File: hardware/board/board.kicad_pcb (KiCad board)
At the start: 2 copper layers, 100 x 30 mm, 40 parts, among them J1 DC THRU, J2 DC THRU, J3 DC OUT, J4 DC IN, J5 DC IN, J6 DC OUT, J7 Eurorack Power, J8 Eurorack Power, SW1 ON/OFF, U1 VX7805-500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

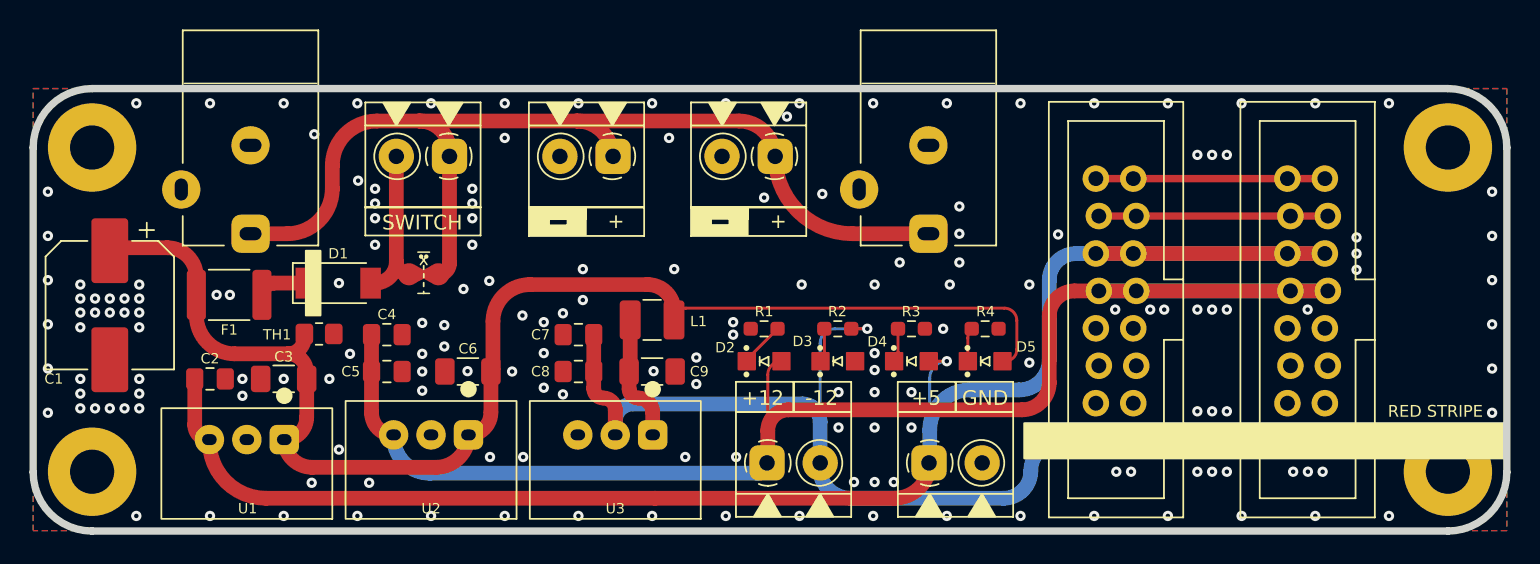
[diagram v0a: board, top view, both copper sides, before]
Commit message: Use new winterbloom footprints
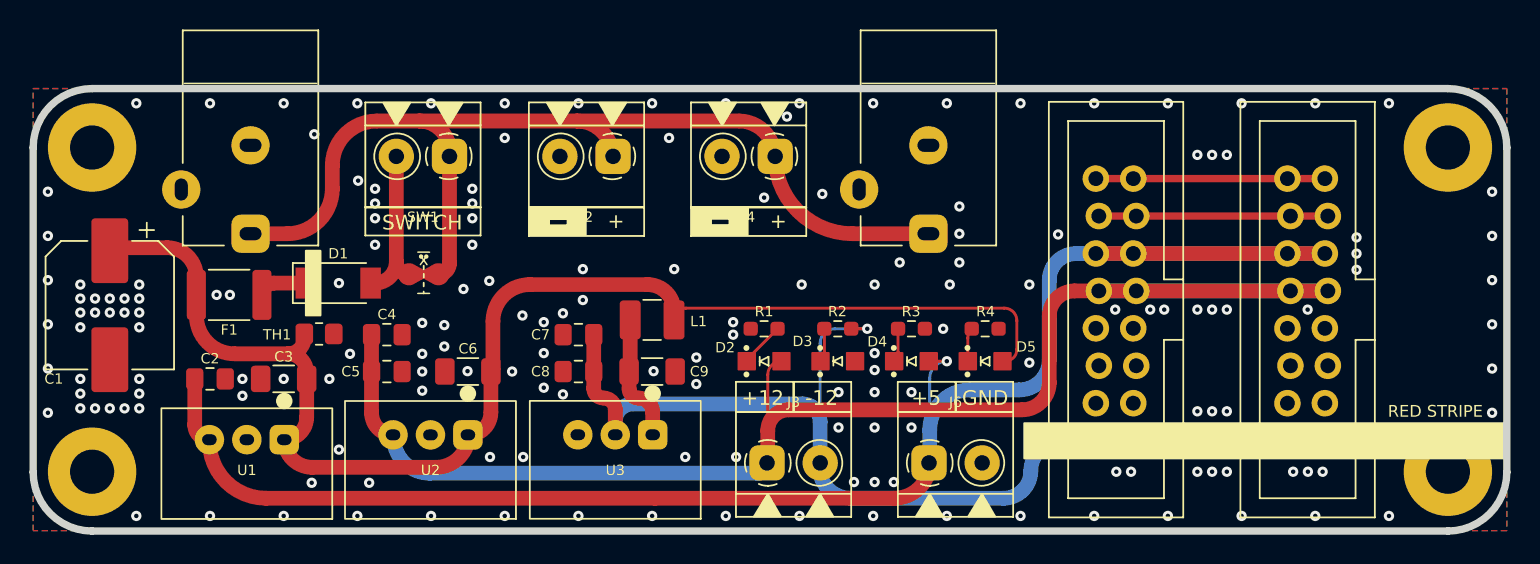
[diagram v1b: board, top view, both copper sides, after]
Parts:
- J2, J3, J4, J6, SW1: footprint winterbloom:TerminalBlock_4Ucon_1x02_P3.50mm_Horizontal -> winterbloom:TerminalBlock_4UCON_1x02_P3.50mm_Horizontal
- J7, J8: footprint winterbloom:IDC-Header_2x08_P2.54mm_Vertical_Press_Fit -> winterbloom:Eurorack_Power_2x8_Shrouded_Lock
- U1: footprint winterbloom:CUI_VX78 -> winterbloom:Converter_DCDC_CUI_VX78-500_THT
- U2, U3: footprint winterbloom:CUI_P78E -> winterbloom:Converter_DCDC_CUI_P78E-1000_THT
- moved U3 3.06 mm to (100.5, 116.6)
- moved U2 3.02 mm to (88.0, 116.6)
- moved U1 3.01 mm to (75.5, 116.9)

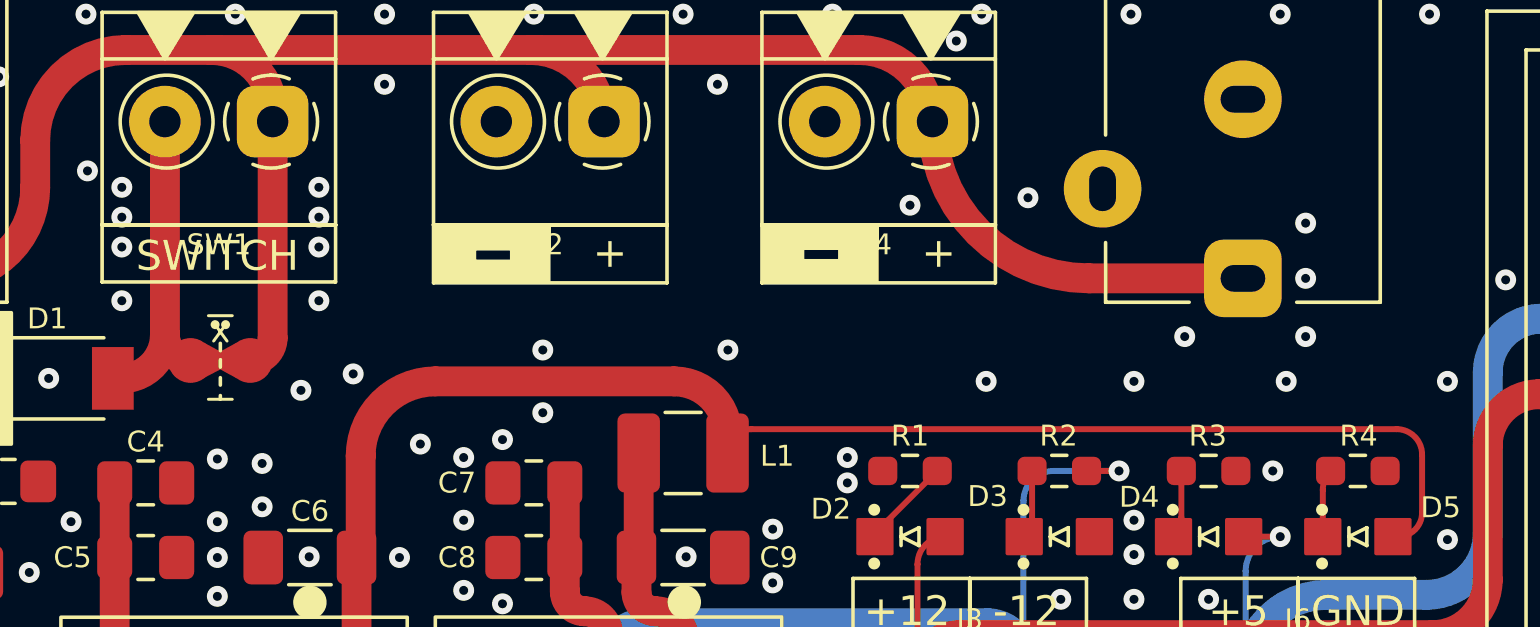
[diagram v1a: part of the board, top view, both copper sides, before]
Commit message: Add OSHW and polarity symbols to the PCB
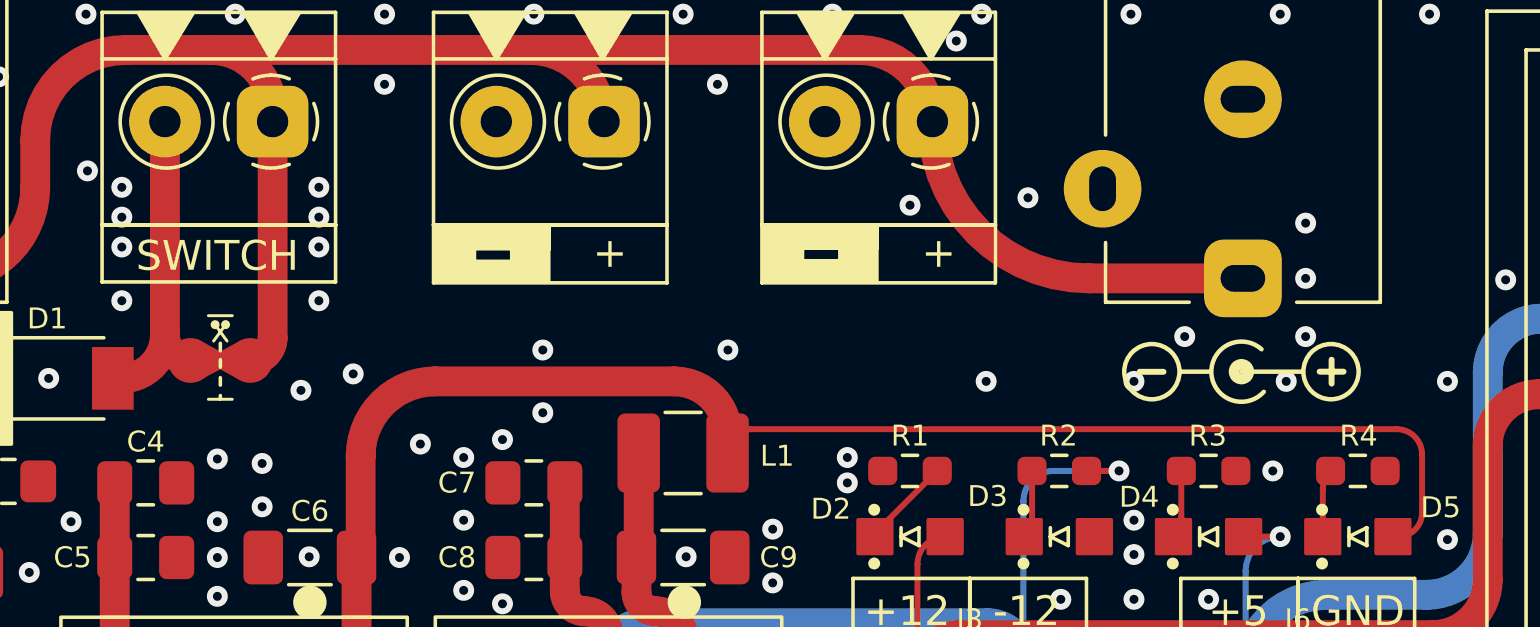
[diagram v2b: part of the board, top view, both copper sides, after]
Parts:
- added REF**: Symbol_Barrel_Polarity, Symbol:Symbol_Barrel_Polarity, F.Cu at (119.2, 106.0)
- added REF**: OSHW-Logo_5.7x6mm_Copper, Symbol:OSHW-Logo_5.7x6mm_Copper, B.Cu at (153.9, 108.5)
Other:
- board text removed: "TRANS RIGHTS"

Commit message: Resolve ERC errors related to non-schematic footprints
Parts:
- renumbered G*** to NICKEL, REF** to OSHW, REF** to POLARITY, G*** to WNTR
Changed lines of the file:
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@@
     (tags "barrel polarity")
     (attr board_only exclude_from_pos_files exclude_from_bom)
-    (fp_text reference "REF**" (at 0 -2) (layer "F.SilkS") hide
+    (fp_text reference "POLARITY" (at 0 -2) (layer "F.SilkS") hide
       (effects (font (size 1 1) (thickness 0.15)))
     )
@@
     (at 105.4 108.075 180)
     (attr board_only exclude_from_pos_files exclude_from_bom)
-    (fp_text reference "G***" (at 0 0) (layer "B.SilkS") hide
+    (fp_text reference "WNTR" (at 0 0) (layer "B.SilkS") hide
       (effects (font (size 1.524 1.524) (thickness 0.3)) (justify mirror))
     )
@@
     (at 65.1 108.075 180)
     (attr board_only exclude_from_pos_files exclude_from_bom)
-    (fp_text reference "G***" (at 0 0) (layer "B.SilkS") hide
+    (fp_text reference "NICKEL" (at 0 0) (layer "B.SilkS") hide
       (effects (font (size 1.524 1.524) (thickness 0.3)) (justify mirror))
     )
@@
     (descr "Open Source Hardware Logo")
     (tags "Logo OSHW")
-    (attr exclude_from_pos_files exclude_from_bom)
-    (fp_text reference "REF**" (at 0 0) (layer "B.SilkS") hide
+    (attr board_only exclude_from_pos_files exclude_from_bom)
+    (fp_text reference "OSHW" (at 0 0) (layer "B.SilkS") hide
       (effects (font (size 1 1) (thickness 0.15)) (justify mirror))
     )

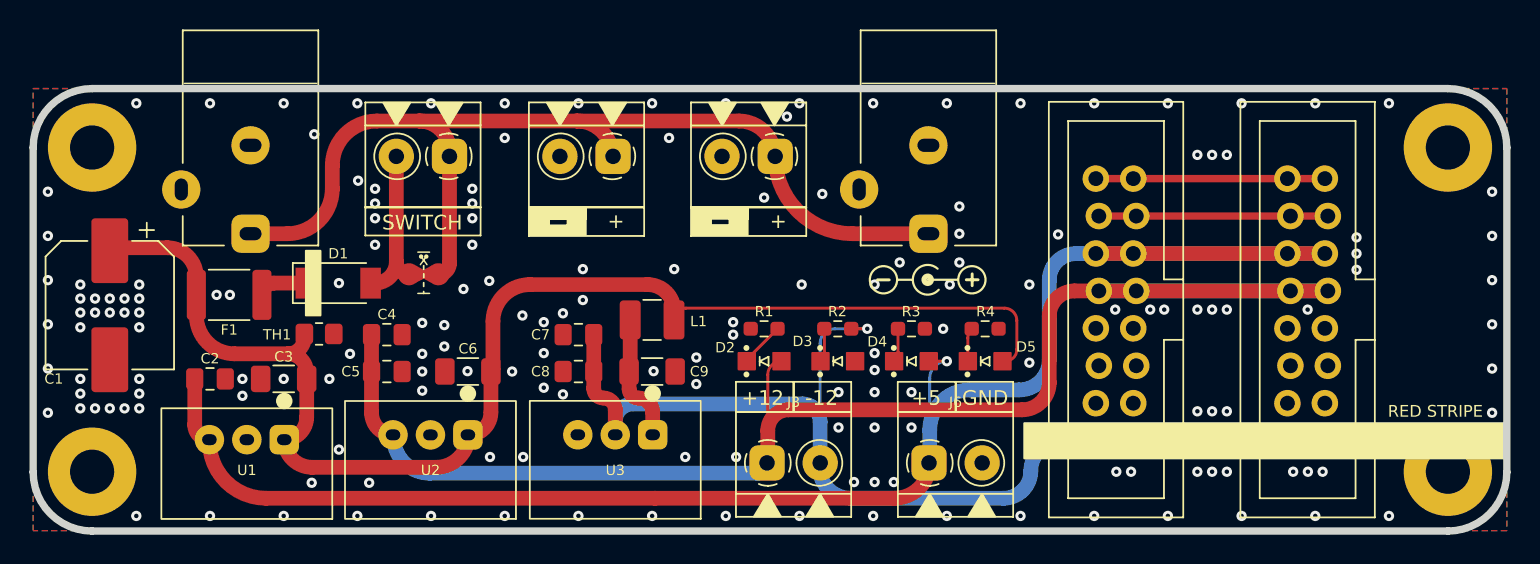
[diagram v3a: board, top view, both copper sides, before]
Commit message: Use hatched fills
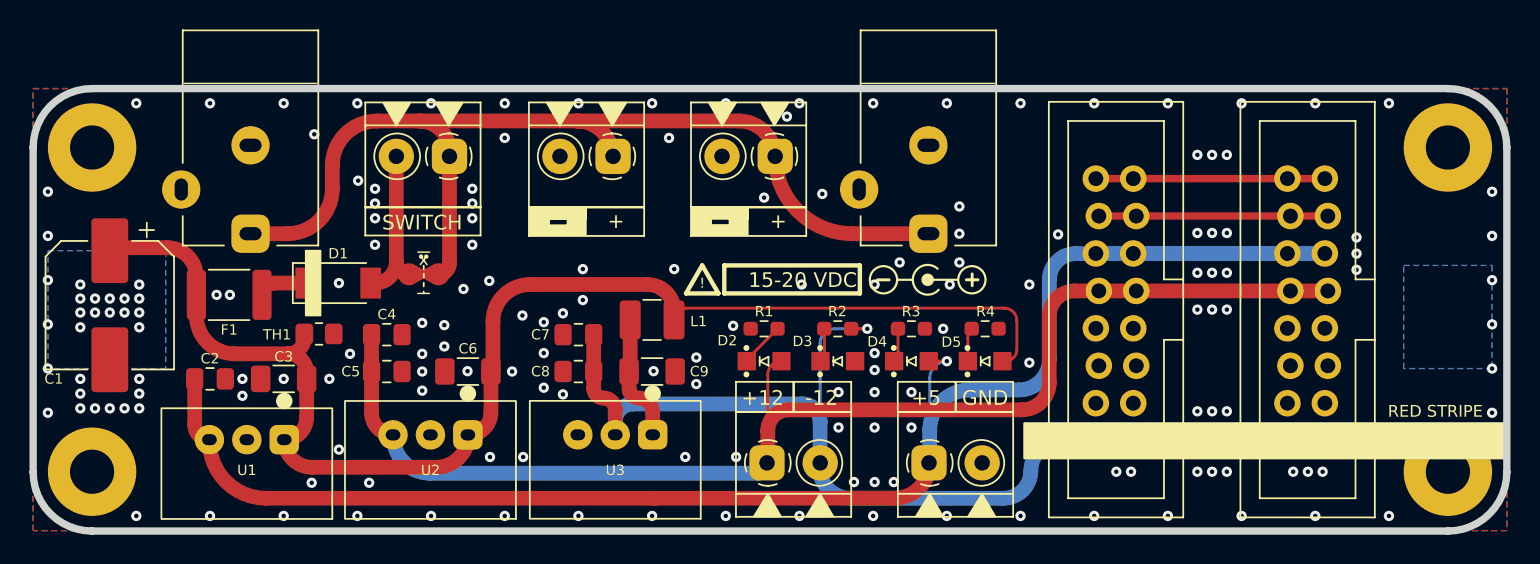
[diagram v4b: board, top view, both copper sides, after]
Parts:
- removed NICKEL: LOGO, LOGO
- added G***: LOGO, LOGO, B.Cu at (63.5, 108.1)
- C2: value 22uF/10V -> 22uF/25V
- C5, C8: value 4.7uF -> 4.7uF/25V
- R1, R2, R4: value 5k -> 5.1k
- R3: value 1k/5k -> 5.1k
- U2, U3: value P78E-1000 -> P78E12-1000
- moved OSHW 0.55 mm to (154.5, 108.5)
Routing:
- net +12V: track 101.9 -> 86.4 mm
- net -12V: track 90.0 -> 74.5 mm
- net +5V: track 119.3 -> 103.8 mm
- net GND: vias 172 -> 173
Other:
- board text added: "!"
- board text added: "15-20 VDC"

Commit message: Move some silkscreen around just a little
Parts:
- moved POLARITY 14.1 mm to (105.1, 105.3)
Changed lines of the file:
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@@
   )
   (footprint "Symbol:Symbol_Barrel_Polarity" (layer "F.Cu")
-    (at 119.2 105.975)
+    (at 105.1 105.275)
     (descr "Barrel connector polarity indicator")
     (tags "barrel polarity")
@@
   (gr_poly
     (pts
-      (xy 105 106.975)
-      (xy 102.8 106.975)
-      (xy 103.9 105.075)
+      (xy 90.9 106.275)
+      (xy 88.7 106.275)
+      (xy 89.8 104.375)
     ) (layer "F.SilkS") (width 0.3) (fill none))
   (gr_rect (start 103.14 101.135) (end 107.05 101.975) (layer "F.SilkS") (width 0) (fill solid))
@@
   (gr_rect (start 103.14 103.075) (end 110.96 101.135) (layer "F.SilkS") (width 0.12) (fill none))
   (gr_rect (start 92.15 101.155) (end 96.06 101.995) (layer "F.SilkS") (width 0) (fill solid))
-  (gr_rect (start 105.4 105.075) (end 114.6 106.975) (layer "F.SilkS") (width 0.3) (fill none))
+  (gr_rect (start 91.3 104.375) (end 100.5 106.275) (layer "F.SilkS") (width 0.3) (fill none))
   (gr_rect (start 105.69 101.135) (end 107.05 103.05) (layer "F.SilkS") (width 0) (fill solid))
   (gr_line (start 58.5 108.075) (end 158.5 108.075) (layer "Dwgs.User") (width 0.1))
@@
     (effects (font (size 1 1) (thickness 0.2)))
   )
-  (gr_text "15-20 VDC" (at 114.4 106.075) (layer "F.SilkS")
+  (gr_text "15-20 VDC" (at 100.3 105.375) (layer "F.SilkS")
     (effects (font (size 1 1) (thickness 0.15)) (justify right))
   )
@@
     (effects (font (size 1 1) (thickness 0.2)))
   )
-  (gr_text "!" (at 103.9 106.275) (layer "F.SilkS")
+  (gr_text "!" (at 89.8 105.575) (layer "F.SilkS")
     (effects (font (size 0.7 0.7) (thickness 0.15)))
   )

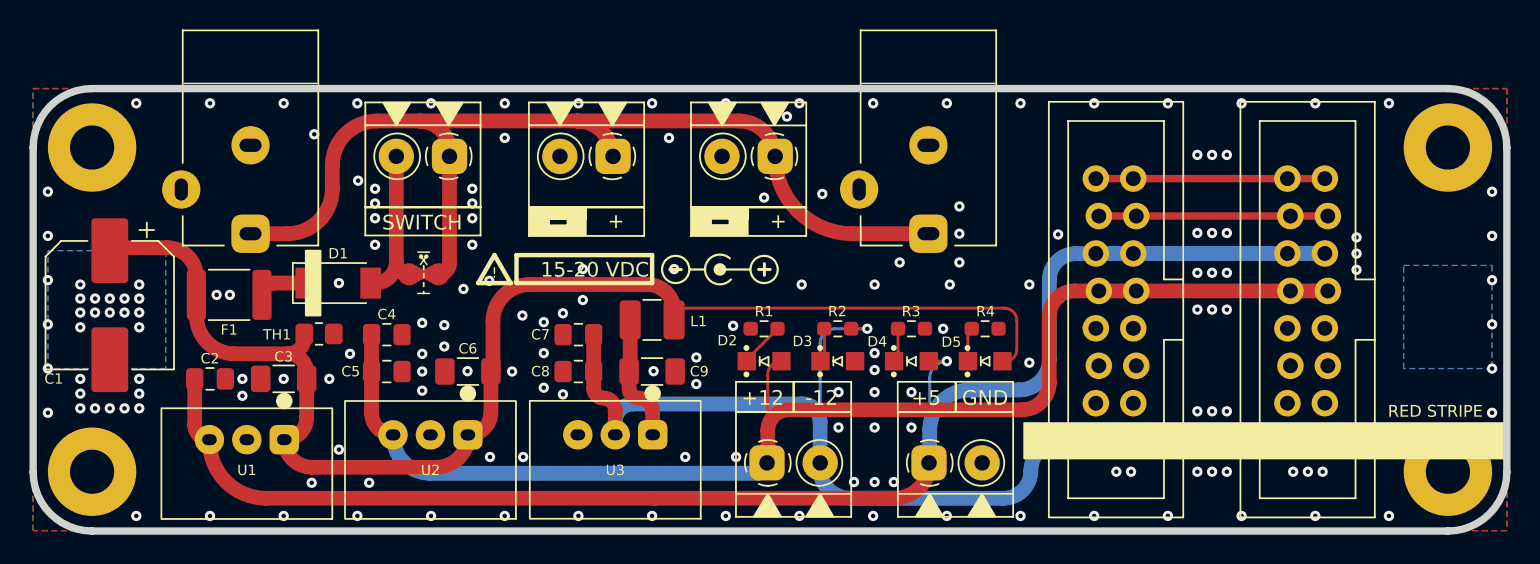
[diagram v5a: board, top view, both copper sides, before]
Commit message: Update the PCB with the new name
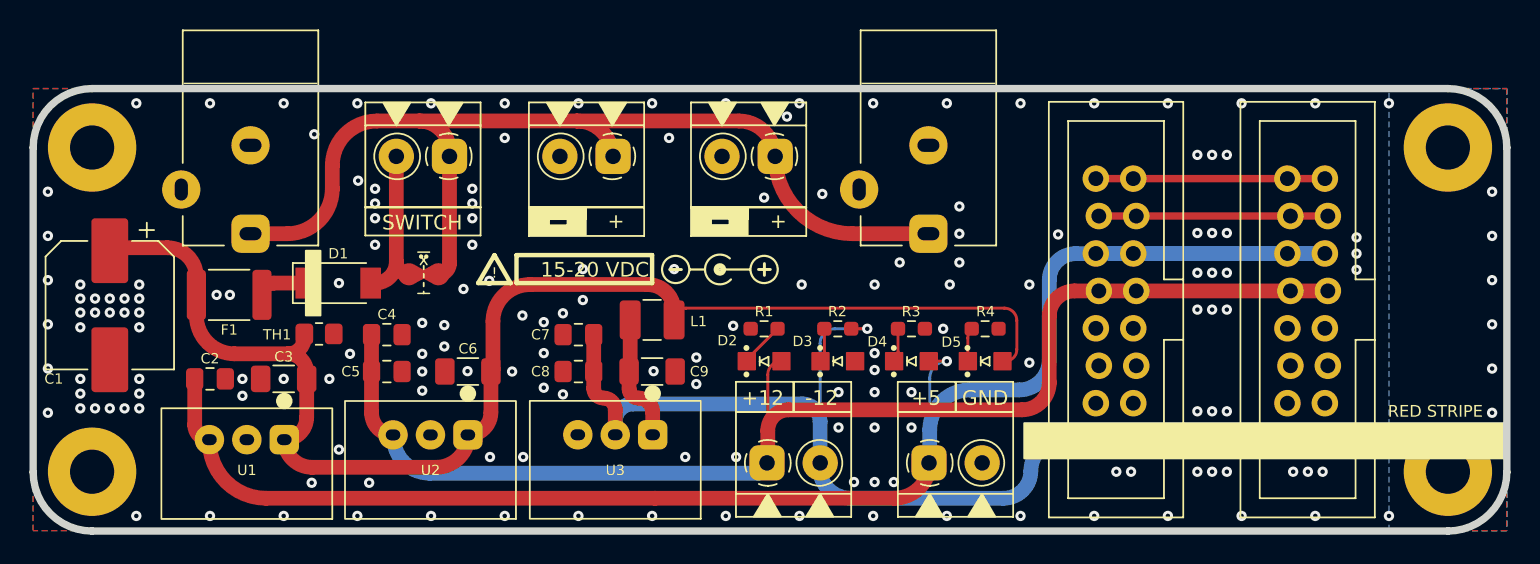
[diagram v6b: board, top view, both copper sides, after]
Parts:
- removed G***: LOGO, LOGO
- C1: value 100uF/50V -> 100u
- C2, C4, C7: value 22uF/25V -> 22u
- C3, C6, C9: value 10uF/50V -> 10u
- C5, C8: value 4.7uF/25V -> 4.7u
- D1: value 3A BARRIER -> BARRIER
- F1: value Polyfuse -> 1.5A
- TH1: value 18V MOV -> MOV
- moved OSHW 2.55 mm to (154.5, 111.1)
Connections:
- net /DCIN renamed +15V
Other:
- board text added: "TRANS RIGHTS"
